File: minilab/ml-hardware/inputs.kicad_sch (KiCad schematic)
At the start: 19 parts, among them U3 4049

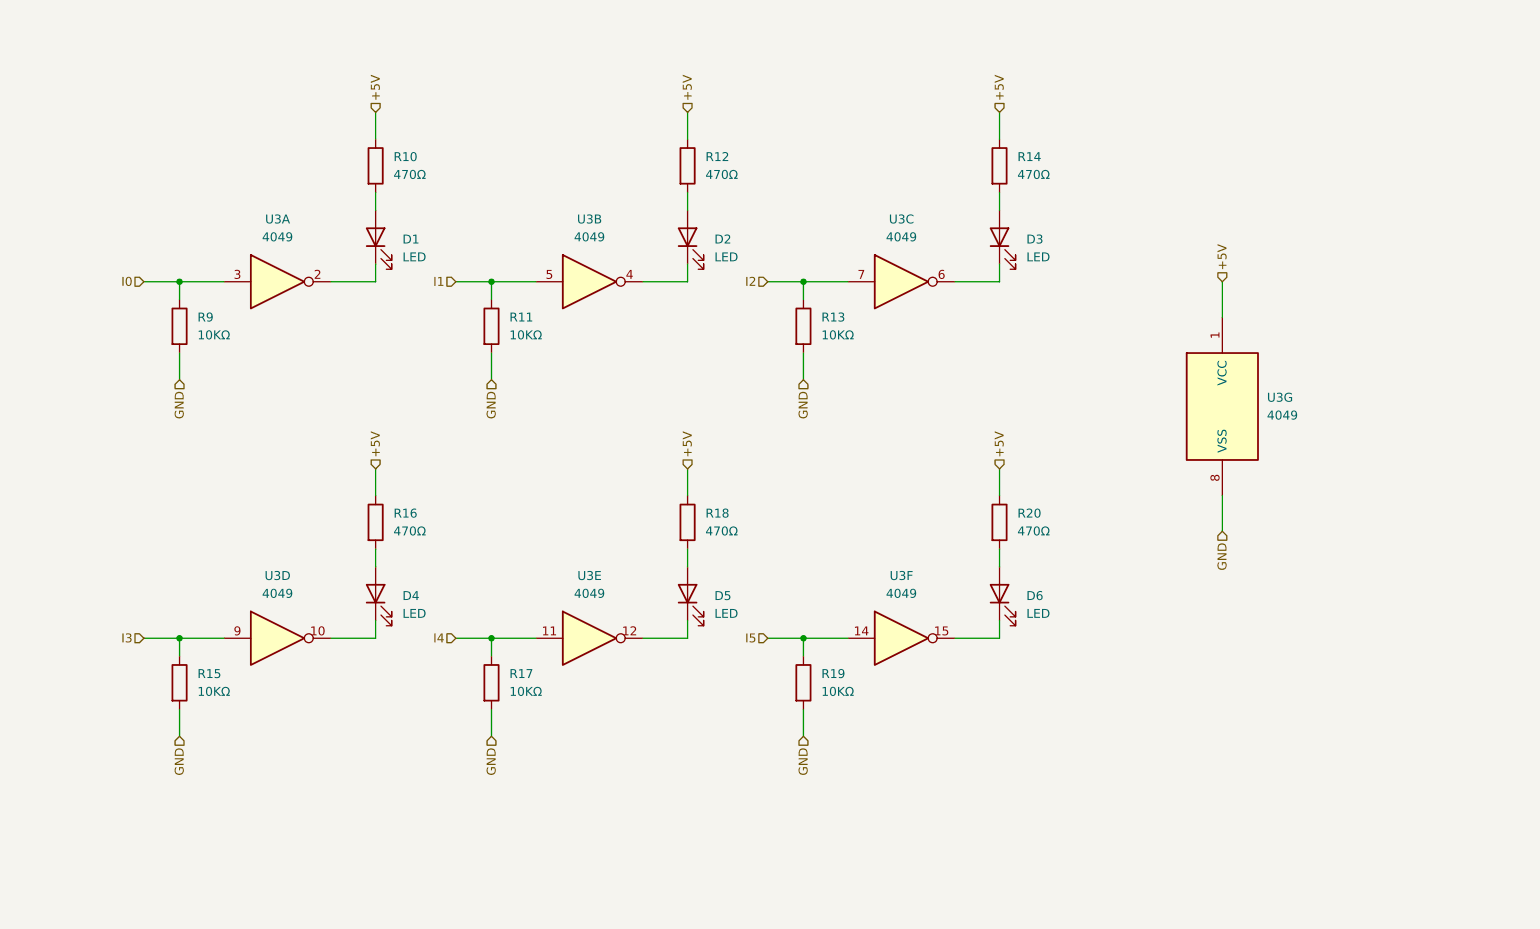
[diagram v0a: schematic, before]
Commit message: minilab: change 4096 to 74HC540 for 1byte input
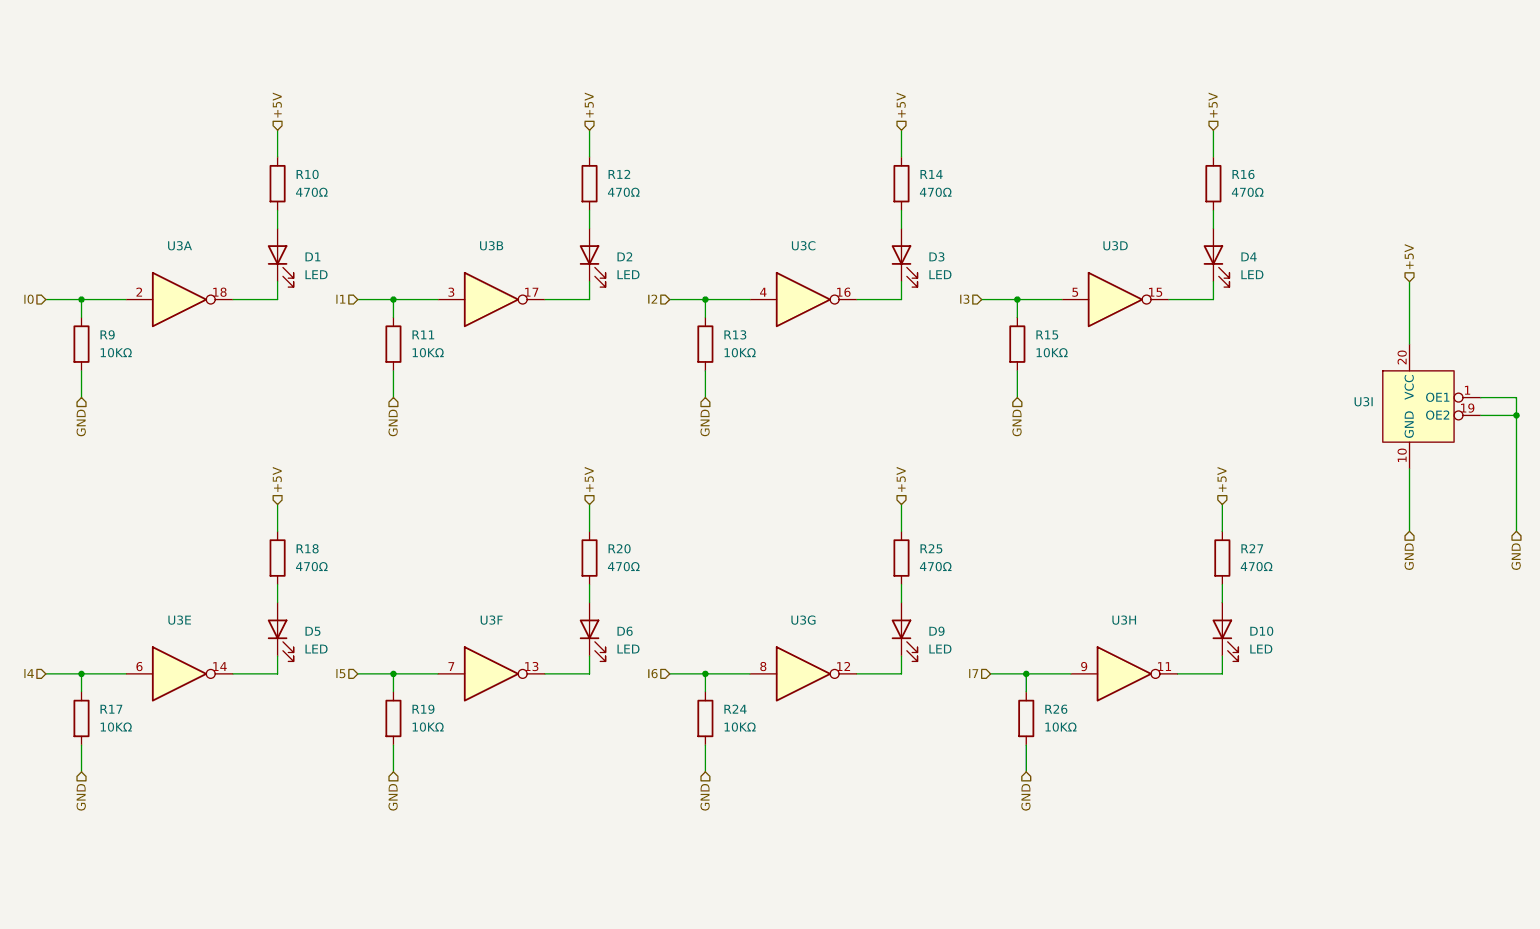
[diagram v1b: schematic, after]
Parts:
- removed U3: 4049, symbol 4xxx:4049
- added D10, D9: LED, symbol Device:LED
- added R24, R26: 10KΩ, symbol Device:R
- added R25, R27: 470Ω, symbol Device:R
- added U3: ~, symbol Extras:74HC540N
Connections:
- net +5V: now also R25.1, R27.1, U3.20 (VCC)
- net GND: now also R24.2, R26.2, U3.1 (OE1), U3.10 (GND), U3.19 (OE2)
- net I0: now also U3.2
- net I1: now also U3.3
- net I2: now also U3.4
- net I3: now also U3.5
- net I4: now also U3.6
- net I5: now also U3.7
- net at D6.1 (K): now also U3.13
- net at D5.1 (K): now also U3.14
- net at D4.1 (K): now also U3.15
- net at D3.1 (K): now also U3.16
- net at D2.1 (K): now also U3.17
- net at D1.1 (K): now also U3.18
- new net: D10.1 (K), U3.11
- new net: D10.2 (A), R27.2
- new net: D9.1 (K), U3.12
- new net: D9.2 (A), R25.2
- new net I6: R24.1, U3.8
- new net I7: R26.1, U3.9
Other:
- moved on the sheet: D1, D2, D3, D4, D5, D6, R10, R11, R12, R13, R14, R15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

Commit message: minilab: Enforce "pcb/page" hierarchy on schematic
This does not apply (necessarily) to subpages.
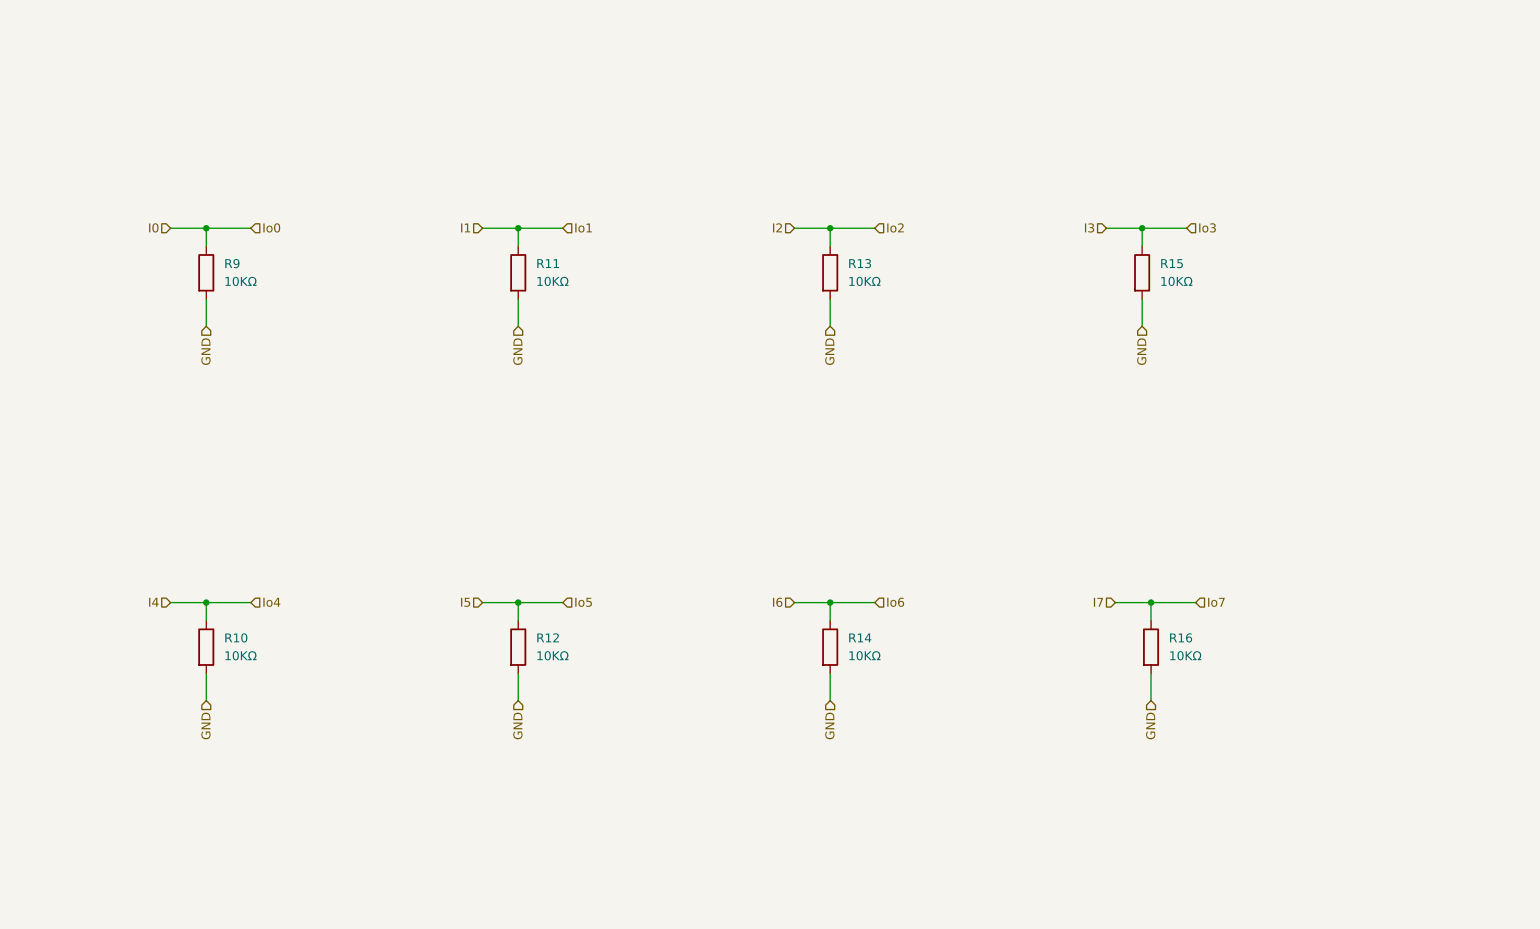
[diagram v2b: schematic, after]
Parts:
- removed D1, D10, D2, D3, D4, D5, D6, D9: LED, symbol Device:LED
- removed R10, R12, R14, R16, R18, R20, R25, R27: 470Ω, symbol Device:R
- removed U3: ~, symbol Extras:74HC540N
- R10: renamed from R17; footprint (none) -> Resistor_THT:R_Axial_DIN0204_L3.6mm_D1.6mm_P5.08mm_Horizontal
- R11, R13, R15, R9: footprint (none) -> Resistor_THT:R_Axial_DIN0204_L3.6mm_D1.6mm_P5.08mm_Horizontal
- R12: renamed from R19; footprint (none) -> Resistor_THT:R_Axial_DIN0204_L3.6mm_D1.6mm_P5.08mm_Horizontal
- R14: renamed from R24; footprint (none) -> Resistor_THT:R_Axial_DIN0204_L3.6mm_D1.6mm_P5.08mm_Horizontal
- R16: renamed from R26; footprint (none) -> Resistor_THT:R_Axial_DIN0204_L3.6mm_D1.6mm_P5.08mm_Horizontal
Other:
- moved on the sheet: R10, R11, R12, R13, R14, R15, R16, R9

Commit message: minilab: Agrega 2da opc conectores y modelos 3d
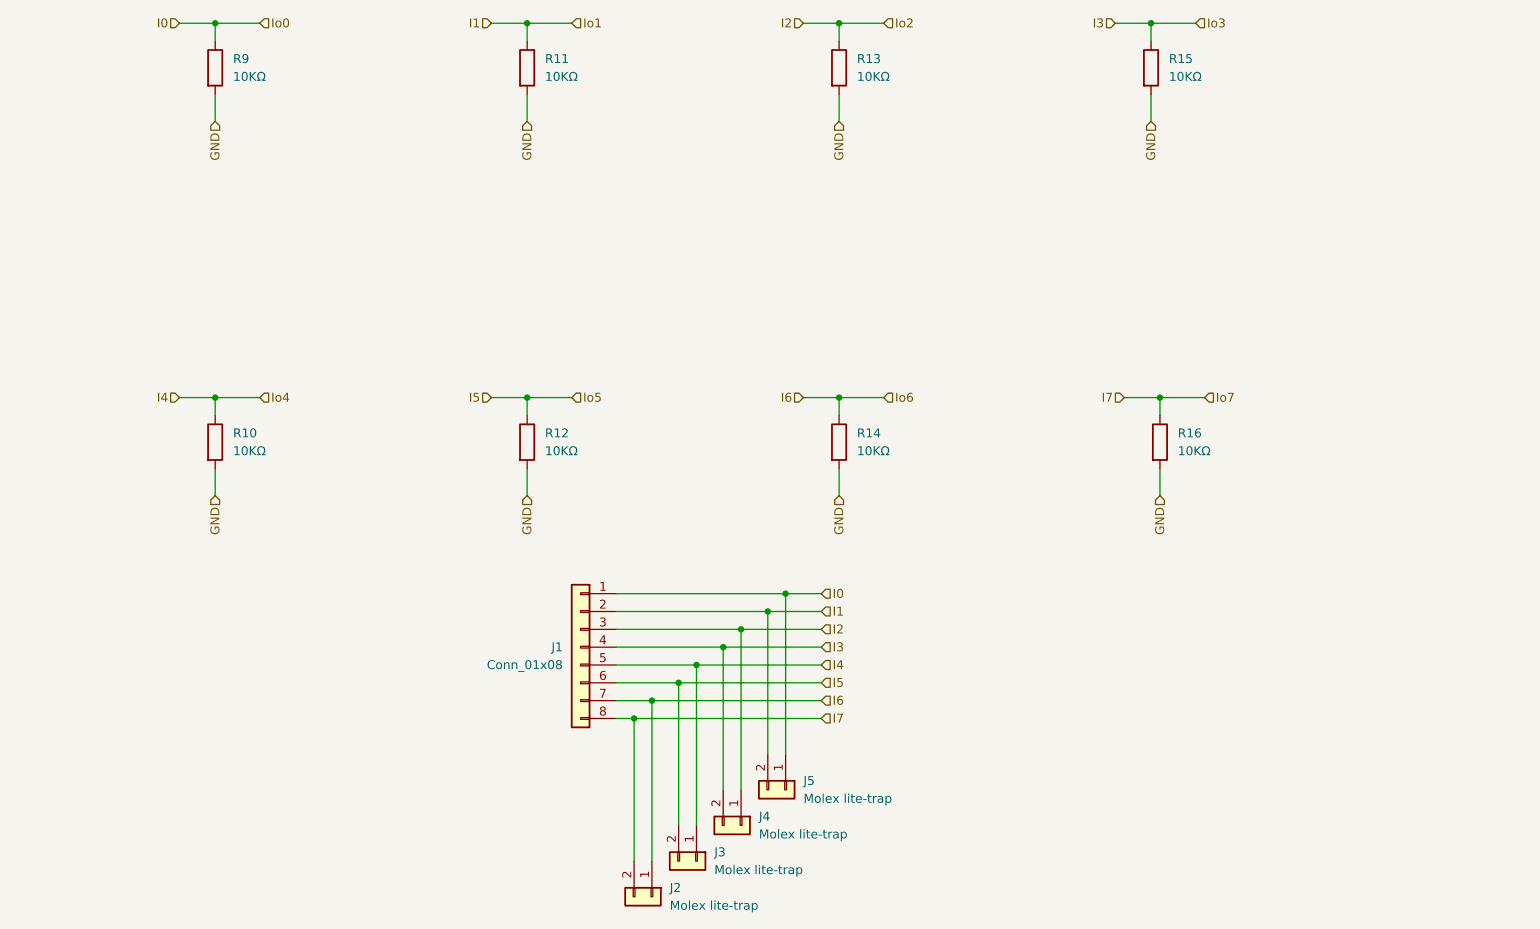
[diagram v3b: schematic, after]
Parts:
- added J1: Conn_01x08, Connector_PinSocket_2.54mm:PinSocket_1x08_P2.54mm_Horizontal, symbol Connector_Generic:Conn_01x08
- added J2, J3, J4, J5: Molex lite-trap, Extras:104238-0210, symbol Connector_Generic:Conn_01x02
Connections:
- net I0: now also J1.1 (Pin_1), J5.1 (Pin_1)
- net I1: now also J1.2 (Pin_2), J5.2 (Pin_2)
- net I2: now also J1.3 (Pin_3), J4.1 (Pin_1)
- net I3: now also J1.4 (Pin_4), J4.2 (Pin_2)
- net I4: now also J1.5 (Pin_5), J3.1 (Pin_1)
- net I5: now also J1.6 (Pin_6), J3.2 (Pin_2)
- net I6: now also J1.7 (Pin_7), J2.1 (Pin_1)
- net I7: now also J1.8 (Pin_8), J2.2 (Pin_2)
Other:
- moved on the sheet: R10, R11, R12, R13, R14, R15, R16, R9

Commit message: minilab: Corrige huella molex microfit y edge-*-02
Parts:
- J2, J3, J4, J5: footprint Extras:104238-0210 -> Extras:Molex-Lite_trap
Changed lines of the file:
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@@
 			)
 		)
-		(property "Footprint" "Extras:104238-0210"
+		(property "Footprint" "Extras:Molex-Lite_trap"
 			(at 147.32 151.13 0)
 			(effects
@@
 			)
 		)
-		(property "Footprint" "Extras:104238-0210"
+		(property "Footprint" "Extras:Molex-Lite_trap"
 			(at 140.97 156.21 0)
 			(effects
@@
 			)
 		)
-		(property "Footprint" "Extras:104238-0210"
+		(property "Footprint" "Extras:Molex-Lite_trap"
 			(at 153.67 146.05 0)
 			(effects
@@
 			)
 		)
-		(property "Footprint" "Extras:104238-0210"
+		(property "Footprint" "Extras:Molex-Lite_trap"
 			(at 134.62 161.29 0)
 			(effects
